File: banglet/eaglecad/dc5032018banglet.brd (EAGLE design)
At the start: 39.8 x 22.6 mm, 39 parts, among them Q3 DMG3415U-7, U2 AP2112(3.3V), U3 MCP73831T-2ACI/OT, U4 CP2104, X1 32.768, X2 JSTPH, X4 20329

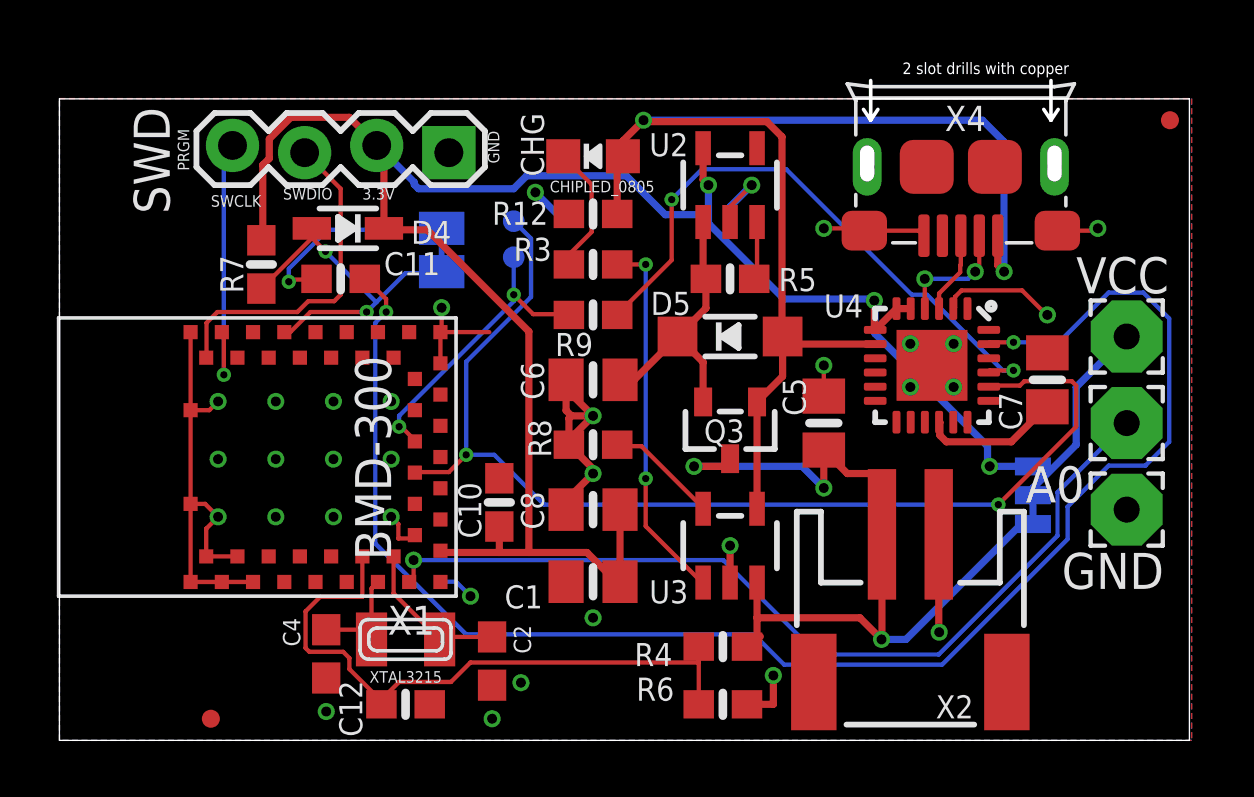
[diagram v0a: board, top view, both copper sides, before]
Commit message: remove some vias under bmd-300 move vias close to bmd-300 pads further away fix shorting of net with solder jumper make usb data line not quite right angle Make a0 a little less close to pads
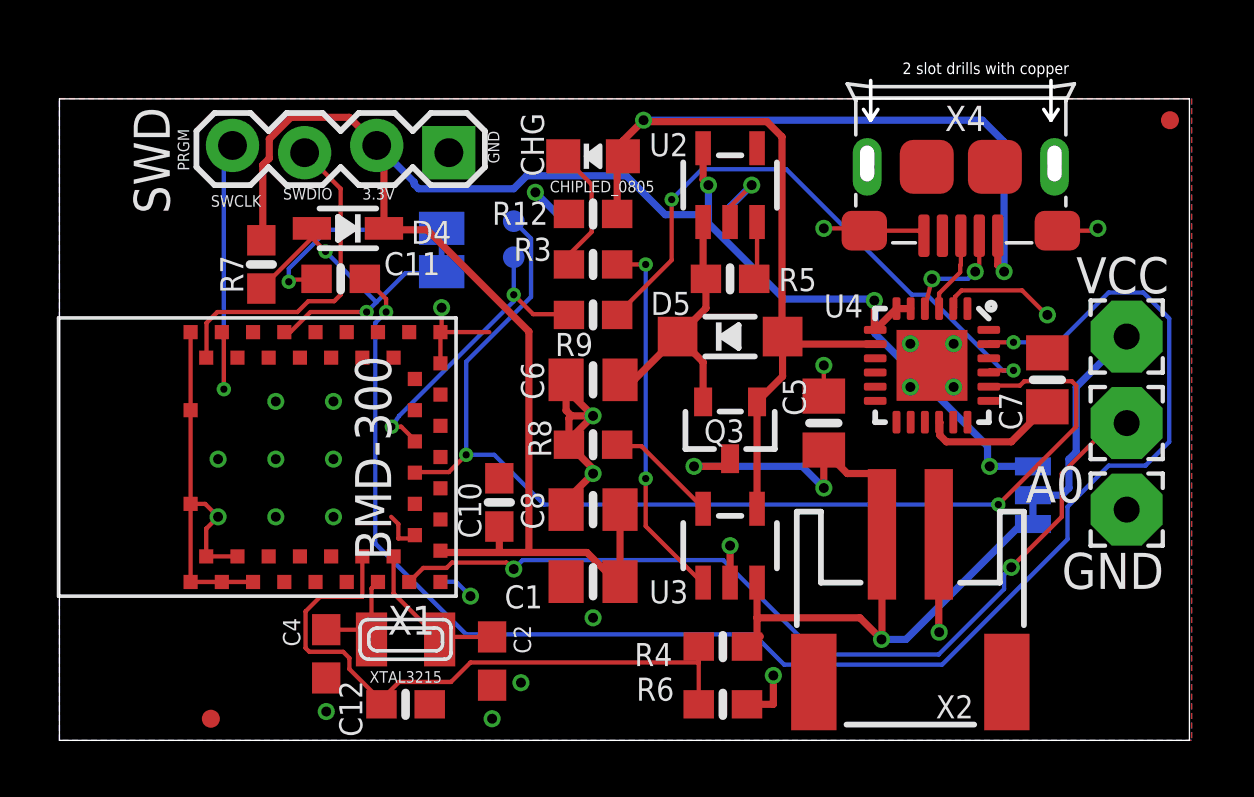
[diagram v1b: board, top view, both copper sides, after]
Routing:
- net N$3: track 6.96 -> 8.62 mm
- net GND: track 53.7 -> 52.6 mm, vias 33 -> 29
- net SWCLK: track 9.74 -> 10.8 mm
- net A0: track 31.6 -> 31.9 mm, vias 1 -> 2
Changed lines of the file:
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@@
 <setting verticaltext="up"/>
 </settings>
-<grid distance="10" unitdist="mil" unit="mil" style="lines" multiple="1" display="no" altdistance="1" altunitdist="mil" altunit="mil"/>
+<grid distance="5" unitdist="mil" unit="mil" style="lines" multiple="1" display="no" altdistance="1" altunitdist="mil" altunit="mil"/>
 <layers>
 <layer number="1" name="Top" color="4" fill="1" visible="yes" active="yes"/>
@@
 <contactref element="C4" pad="2"/>
 <contactref element="C2" pad="2"/>
-<via x="5.588" y="43.18" extent="1-16" drill="0.35"/>
 <via x="7.62" y="43.18" extent="1-16" drill="0.35"/>
 <via x="9.652" y="43.18" extent="1-16" drill="0.35"/>
-<via x="11.684" y="43.18" extent="1-16" drill="0.35"/>
-<via x="11.684" y="41.148" extent="1-16" drill="0.35"/>
 <via x="9.652" y="41.148" extent="1-16" drill="0.35"/>
 <via x="7.62" y="41.148" extent="1-16" drill="0.35"/>
@@
 <via x="7.62" y="39.116" extent="1-16" drill="0.35"/>
 <via x="9.652" y="39.116" extent="1-16" drill="0.35"/>
-<via x="11.684" y="39.116" extent="1-16" drill="0.35"/>
 <via x="23.622" y="38.1" extent="1-16" drill="0.35"/>
 <via x="30.988" y="35.052" extent="1-16" drill="0.35"/>
@@
 <wire x1="5.17" y1="37.722" x2="5.17" y2="38.698" width="0.1524" layer="1"/>
 <wire x1="5.17" y1="38.698" x2="5.588" y2="39.116" width="0.1524" layer="1"/>
-<wire x1="4.62" y1="42.872" x2="5.28" y2="42.872" width="0.1524" layer="1"/>
-<wire x1="5.28" y1="42.872" x2="5.588" y2="43.18" width="0.1524" layer="1"/>
 <via x="16.764" y="50.546" extent="1-16" drill="0.35"/>
 <wire x1="30.972" y1="38.498" x2="30.972" y2="35.068" width="0.254" layer="1"/>
@@
 <via x="32.258" y="47.752" extent="1-16" drill="0.35"/>
 <wire x1="32.258" y1="47.752" x2="32.004" y2="47.498" width="0.1524" layer="16"/>
-<wire x1="32.004" y1="47.498" x2="30.48" y2="47.498" width="0.1524" layer="16"/>
-<via x="30.48" y="47.498" extent="1-16" drill="0.35"/>
-<wire x1="30.48" y1="47.498" x2="30.48" y2="46.454" width="0.1524" layer="1"/>
+<wire x1="32.004" y1="47.498" x2="30.734" y2="47.498" width="0.1524" layer="16"/>
+<via x="30.734" y="47.498" extent="1-16" drill="0.35"/>
+<wire x1="30.734" y1="47.498" x2="30.48" y2="46.454" width="0.1524" layer="1"/>
 <wire x1="30.48" y1="46.454" x2="30.484" y2="46.45" width="0.1524" layer="1"/>
 </signal>
@@
 <contactref element="SWD" pad="4"/>
 <contactref element="U1" pad="P43"/>
-<wire x1="5.7912" y1="44.1198" x2="5.7912" y2="45.5676" width="0.1524" layer="1"/>
-<wire x1="5.7912" y1="51.8922" x2="5.7912" y2="44.1198" width="0.1524" layer="16"/>
+<wire x1="5.7912" y1="43.6118" x2="5.7912" y2="45.5676" width="0.1524" layer="1"/>
+<wire x1="5.7912" y1="51.8922" x2="5.7912" y2="43.6118" width="0.1524" layer="16"/>
 <wire x1="6.096" y1="52.197" x2="5.7912" y2="51.8922" width="0.1524" layer="16"/>
 <wire x1="5.7912" y1="45.5676" x2="5.72" y2="45.622" width="0.1524" layer="1"/>
-<via x="5.7912" y="44.1198" extent="1-16" drill="0.254"/>
+<via x="5.7912" y="43.6118" extent="1-16" drill="0.254"/>
 </signal>
 <signal name="A0">
@@
 <contactref element="A0" pad="1"/>
 <wire x1="12.32" y1="36.822" x2="12.4744" y2="36.9764" width="0.1524" layer="1"/>
-<wire x1="12.4744" y1="36.9764" x2="12.4744" y2="37.592" width="0.1524" layer="1"/>
-<via x="12.4744" y="37.592" extent="1-16" drill="0.35"/>
-<wire x1="12.4744" y1="37.592" x2="23.3796125" y2="37.592" width="0.1524" layer="16"/>
-<wire x1="35.1536" y1="39.9796" x2="37.592" y2="42.418" width="0.1524" layer="16"/>
-<wire x1="35.1536" y1="38.4498125" x2="35.1536" y2="39.9796" width="0.1524" layer="16"/>
+<wire x1="16.316" y1="37.592" x2="23.3796125" y2="37.592" width="0.1524" layer="16"/>
 <wire x1="23.3796125" y1="37.592" x2="26.7042125" y2="34.2674" width="0.1524" layer="16"/>
 <wire x1="26.7042125" y1="34.2674" x2="30.9711875" y2="34.2674" width="0.1524" layer="16"/>
-<wire x1="30.9711875" y1="34.2674" x2="35.1536" y2="38.4498125" width="0.1524" layer="16"/>
+<wire x1="13.6376875" y1="37.3164" x2="13.8250875" y2="37.5038" width="0.1524" layer="1"/>
+<wire x1="13.8250875" y1="37.5038" x2="15.748" y2="37.5038" width="0.1524" layer="1"/>
+<wire x1="12.32" y1="36.822" x2="12.8144" y2="37.3164" width="0.1524" layer="1"/>
+<wire x1="12.8144" y1="37.3164" x2="13.6376875" y2="37.3164" width="0.1524" layer="1"/>
+<wire x1="15.748" y1="37.5038" x2="15.9738" y2="37.278" width="0.1524" layer="1"/>
+<wire x1="15.9738" y1="37.278" x2="16.002" y2="37.278" width="0.1524" layer="1"/>
+<via x="16.002" y="37.278" extent="1-16" drill="0.35"/>
+<wire x1="16.002" y1="37.278" x2="16.316" y2="37.592" width="0.1524" layer="16"/>
+<wire x1="30.9711875" y1="34.2674" x2="33.274" y2="36.5702125" width="0.1524" layer="16"/>
+<wire x1="33.274" y1="37.084" x2="33.528" y2="37.338" width="0.1524" layer="16"/>
+<via x="33.528" y="37.338" extent="1-16" drill="0.35"/>
+<wire x1="33.528" y1="37.338" x2="35.306" y2="39.116" width="0.1524" layer="1"/>
+<wire x1="35.306" y1="39.116" x2="35.306" y2="40.64" width="0.1524" layer="1"/>
+<wire x1="35.306" y1="40.64" x2="37.084" y2="42.418" width="0.1524" layer="1"/>
+<wire x1="37.084" y1="42.418" x2="37.592" y2="42.418" width="0.1524" layer="1"/>
+<wire x1="33.274" y1="36.5702125" x2="33.274" y2="37.084" width="0.1524" layer="16"/>
 </signal>
 <signal name="N$1">
@@
 <contactref element="TP1" pad="P$1"/>
 <wire x1="12.0396" y1="42.291" x2="12.4968" y2="41.8338" width="0.1524" layer="1"/>
-<wire x1="11.9634" y1="42.291" x2="12.0396" y2="42.291" width="0.1524" layer="1"/>
-<wire x1="11.9634" y1="42.672" x2="11.9634" y2="42.291" width="0.1524" layer="16"/>
+<wire x1="11.7094" y1="42.291" x2="12.0396" y2="42.291" width="0.1524" layer="1"/>
+<wire x1="11.9634" y1="42.672" x2="11.7094" y2="42.291" width="0.1524" layer="16"/>
 <wire x1="16.002" y1="46.7106" x2="11.9634" y2="42.672" width="0.1524" layer="16"/>
 <wire x1="16.002" y1="48.26" x2="16.002" y2="46.9392" width="0.1524" layer="16"/>
@@
 <wire x1="16.002" y1="46.9392" x2="16.6878" y2="46.2534" width="0.1524" layer="1"/>
 <wire x1="17.907" y1="46.2534" x2="17.946" y2="46.228" width="0.1524" layer="1"/>
-<via x="11.9634" y="42.291" extent="1-16" drill="0.254"/>
+<via x="11.7094" y="42.291" extent="1-16" drill="0.254"/>
 <via x="16.002" y="46.9392" extent="1-16" drill="0.254"/>
 </signal>
@@
 <wire x1="35.814" y1="43.7388" x2="35.6616" y2="43.8912" width="0.1524" layer="1"/>
 <wire x1="35.814" y1="42.291" x2="35.814" y2="43.7388" width="0.1524" layer="1"/>
-<wire x1="33.0708" y1="39.5478" x2="35.814" y2="42.291" width="0.1524" layer="1"/>
+<wire x1="33.0708" y1="39.5478" x2="34.4805" y2="40.9575" width="0.1524" layer="1"/>
+<wire x1="34.4805" y1="40.9575" x2="35.814" y2="42.291" width="0.1524" layer="1"/>
 <wire x1="17.0688" y1="39.5478" x2="33.0708" y2="39.5478" width="0.1524" layer="16"/>
 <wire x1="15.3162" y1="41.3004" x2="17.0688" y2="39.5478" width="0.1524" layer="16"/>
@@
 <contactref element="JP3" pad="2"/>
 <wire x1="34.29" y1="39.878" x2="34.29" y2="40.132" width="0.254" layer="16"/>
-<wire x1="34.29" y1="40.132" x2="35.814" y2="41.656" width="0.254" layer="16"/>
-<wire x1="35.814" y1="41.656" x2="35.814" y2="43.688" width="0.254" layer="16"/>
-<wire x1="35.814" y1="43.688" x2="37.592" y2="45.466" width="0.254" layer="16"/>
+<wire x1="37.592" y1="45.466" x2="35.814" y2="43.688" width="0.254" layer="16"/>
+<wire x1="35.814" y1="43.688" x2="35.814" y2="41.402" width="0.254" layer="16"/>
+<wire x1="35.814" y1="41.402" x2="35.56" y2="41.148" width="0.254" layer="16"/>
+<wire x1="35.56" y1="41.148" x2="35.56" y2="40.132" width="0.254" layer="16"/>
+<wire x1="35.56" y1="40.132" x2="35.306" y2="39.878" width="0.254" layer="16"/>
+<wire x1="33.8836" y1="39.878" x2="35.306" y2="39.878" width="0.254" layer="16"/>
+<wire x1="34.29" y1="39.878" x2="33.8836" y2="39.878" width="0.1524" layer="16"/>
 </signal>
 </signals>

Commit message: make label for LED strip a little clearer
Move two vias away from bmd pads
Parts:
- renumbered VCC to VLED
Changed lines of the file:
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@@
 <attribute name="VALUE" x="27.838" y="47.204" size="0.4064" layer="27" ratio="10"/>
 </element>
-<element name="VCC" library="wirepad" library_urn="urn:adsk.eagle:library:412" package="2,54/0,9" value="WIREPAD2,54/0,9" x="37.592" y="45.466" smashed="yes">
-<attribute name="NAME" x="35.814" y="46.99" size="1.27" layer="25" ratio="10"/>
+<element name="VLED" library="wirepad" library_urn="urn:adsk.eagle:library:412" package="2,54/0,9" value="WIREPAD2,54/0,9" x="37.592" y="45.466" smashed="yes">
+<attribute name="NAME" x="34.544" y="46.99" size="1.27" layer="25" ratio="10"/>
 <attribute name="VALUE" x="37.592" y="46.066" size="0.0254" layer="27"/>
 </element>
@@
 <wire x1="8.1534" y1="45.6438" x2="7.9248" y2="45.6438" width="0.1524" layer="1"/>
 <wire x1="8.8392" y1="46.3296" x2="8.1534" y2="45.6438" width="0.1524" layer="1"/>
-<wire x1="10.8204" y1="46.3296" x2="8.8392" y2="46.3296" width="0.1524" layer="1"/>
+<wire x1="10.5664" y1="46.4566" x2="8.8392" y2="46.3296" width="0.1524" layer="1"/>
 <wire x1="12.192" y1="47.7012" x2="11.1633" y2="46.6725" width="0.1524" layer="16"/>
-<wire x1="11.1633" y1="46.6725" x2="10.8204" y2="46.3296" width="0.1524" layer="16"/>
+<wire x1="11.1633" y1="46.6725" x2="10.5664" y2="46.4566" width="0.1524" layer="16"/>
 <wire x1="13.4112" y1="47.7012" x2="12.192" y2="47.7012" width="0.1524" layer="16"/>
 <wire x1="7.9248" y1="45.6438" x2="7.92" y2="45.622" width="0.1524" layer="1"/>
@@
 <wire x1="11.1633" y1="46.6725" x2="9.3726" y2="48.4632" width="0.1524" layer="16"/>
 <wire x1="8.9154" y1="48.9204" x2="8.89" y2="49.276" width="0.1524" layer="1"/>
-<via x="10.8204" y="46.3296" extent="1-16" drill="0.254"/>
+<via x="10.5664" y="46.4566" extent="1-16" drill="0.254"/>
 <via x="9.3726" y="48.4632" extent="1-16" drill="0.254"/>
 </signal>
@@
 <wire x1="11.1252" y1="38.1762" x2="14.3256" y2="34.9758" width="0.1524" layer="16"/>
 <wire x1="11.1252" y1="45.9486" x2="11.1252" y2="38.1762" width="0.1524" layer="16"/>
-<wire x1="11.5062" y1="46.3296" x2="11.1252" y2="45.9486" width="0.1524" layer="16"/>
-<wire x1="11.5062" y1="46.7868" x2="11.5062" y2="46.3296" width="0.1524" layer="1"/>
+<wire x1="11.7602" y1="46.4566" x2="11.1252" y2="45.9486" width="0.1524" layer="16"/>
+<wire x1="11.5062" y1="46.7868" x2="11.7602" y2="46.4566" width="0.1524" layer="1"/>
 <wire x1="10.8204" y1="47.4726" x2="11.5062" y2="46.7868" width="0.1524" layer="1"/>
 <wire x1="32.766" y1="45.2628" x2="32.734" y2="45.2" width="0.1524" layer="1"/>
 <wire x1="10.8204" y1="47.4726" x2="10.756" y2="47.498" width="0.1524" layer="1"/>
 <via x="33.6042" y="45.2628" extent="1-16" drill="0.254"/>
-<via x="11.5062" y="46.3296" extent="1-16" drill="0.254"/>
+<via x="11.7602" y="46.4566" extent="1-16" drill="0.254"/>
 </signal>
 <signal name="N$13">
@@
 </signal>
 <signal name="N$3">
-<contactref element="VCC" pad="1"/>
+<contactref element="VLED" pad="1"/>
 <contactref element="JP3" pad="2"/>
 <wire x1="34.29" y1="39.878" x2="34.29" y2="40.132" width="0.254" layer="16"/>
